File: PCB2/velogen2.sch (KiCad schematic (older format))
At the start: 39 parts, among them J1 DYN, J3 AUX0, J4 AUX1, J5 AUX2, J6 BAT, Q1 BSS123, Q2 DMP10H400SE, U1 TPS560200, U2 ESP32-WROOM-32, U3 INA219BxD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

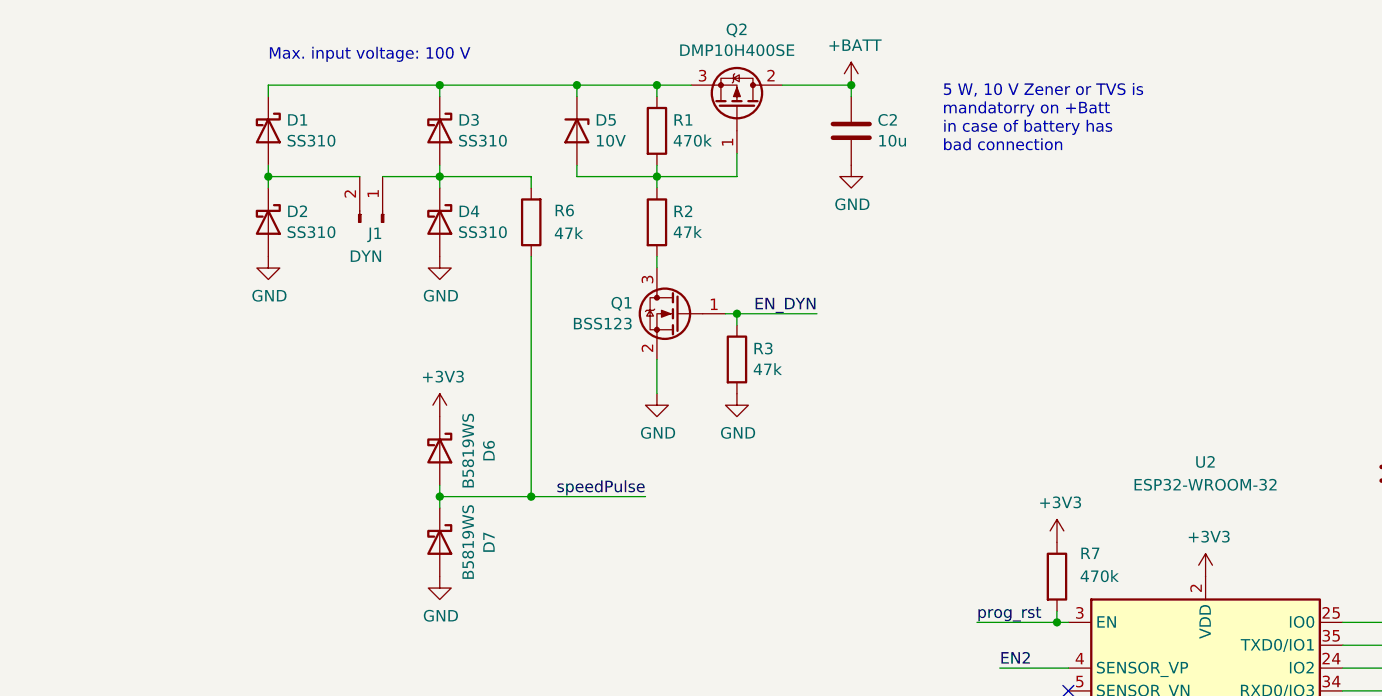
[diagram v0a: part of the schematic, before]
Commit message: invert wakeup pin polarity
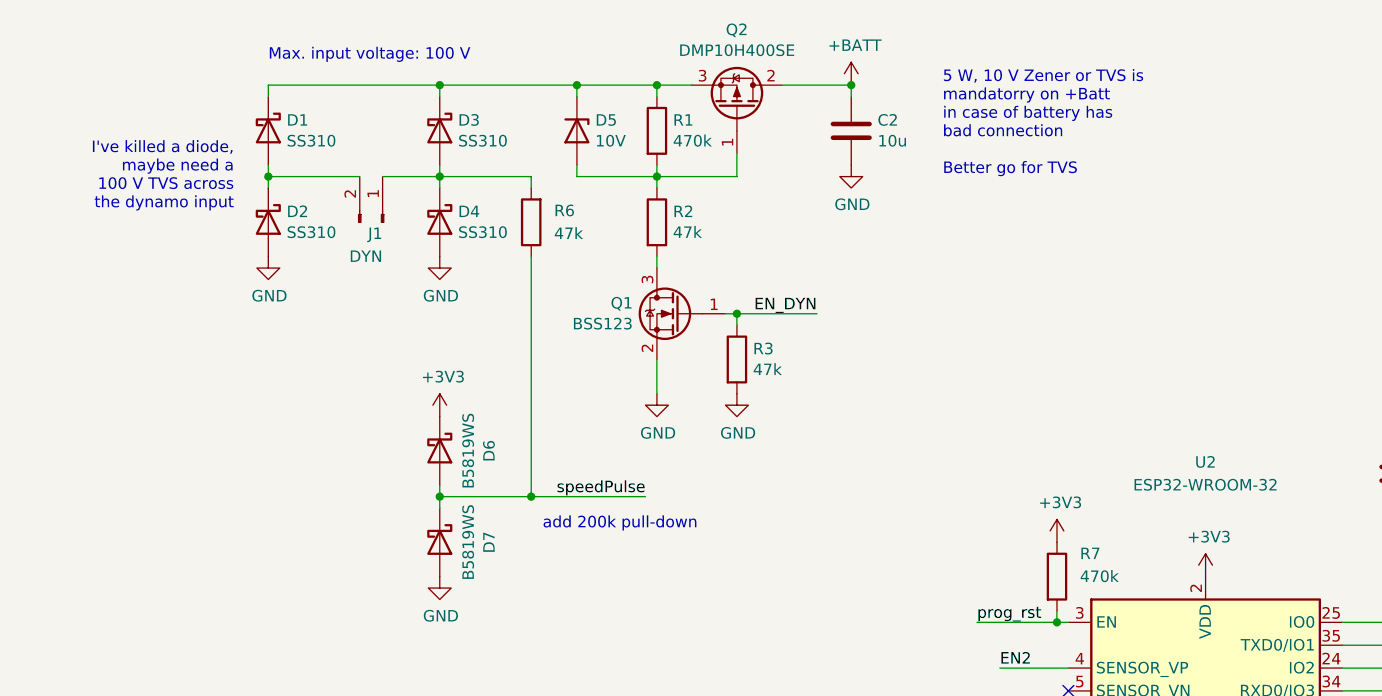
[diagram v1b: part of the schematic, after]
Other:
- note added: "5 W, 10 V Zener or TVS is\nmandatorry on +Batt\nin case of battery has\nbad connection\n\nBetter go for TVS"
- note added: "I've killed a diode,\nmaybe need a\n100 V TVS across \nthe dynamo input"
- note added: "add 200k pull-down"
- note removed: "5 W, 10 V Zener or TVS is\nmandatorry on +Batt\nin case of battery has\nbad connection"
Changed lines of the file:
@@
 Text Notes 6950 1800 0    50   ~ 0
 should be 0603, 10uF
-Text Notes 4500 1500 0    50   ~ 0
-5 W, 10 V Zener or TVS is\nmandatorry on +Batt\nin case of battery has\nbad connection
+Text Notes 4500 1600 0    50   ~ 0
+5 W, 10 V Zener or TVS is\nmandatorry on +Batt\nin case of battery has\nbad connection\n\nBetter go for TVS
+Text Notes 2750 3150 0    50   ~ 0
+add 200k pull-down
+Text Notes 1400 1750 2    50   ~ 0
+I've killed a diode,\nmaybe need a\n100 V TVS across \nthe dynamo input
 $EndSCHEMATC
